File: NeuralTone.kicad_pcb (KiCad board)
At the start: 2 copper layers, 89 parts, among them J1 USB C, J2 Guitar, J3 Headphones, J4 USB Port, J5 Line Out, J6 TF-01A, J7 DF40HC(3.0)-100DS, J8 DF40HC(3.0)-100DS, Q1 AON7421, SW1 SW_Push, U1 AP2125N-3.3, U2 CH224K, U3 MCP6022, U4 AP2125N-3.3, U5 AP2151, U6 NAU8814YG, U7 DRTR5V0U2SR, Y1 OT322512MJBA4SL

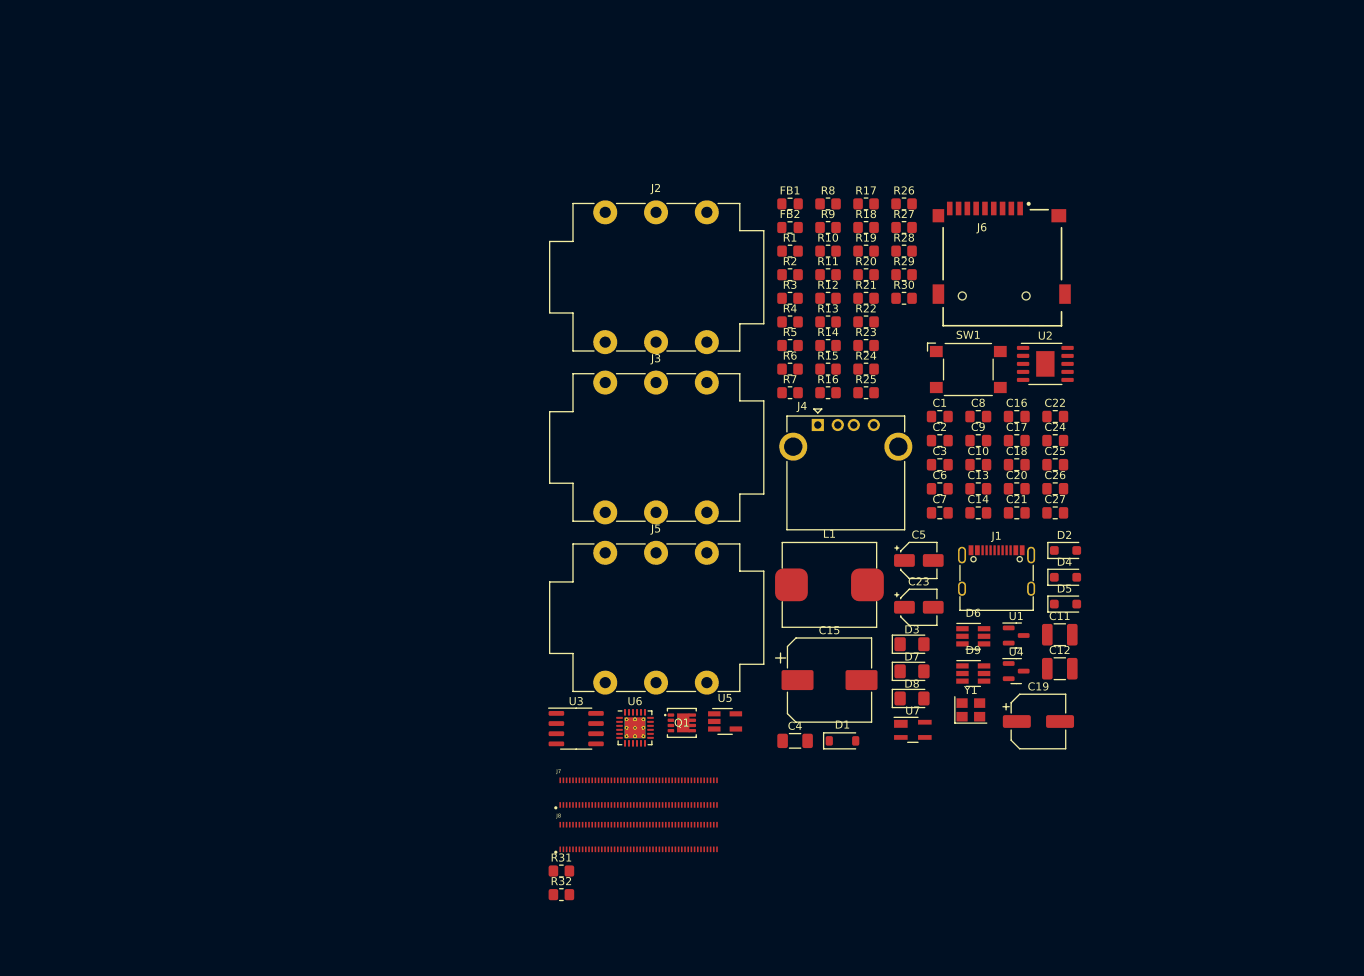
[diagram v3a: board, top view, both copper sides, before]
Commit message: fan control and other updates
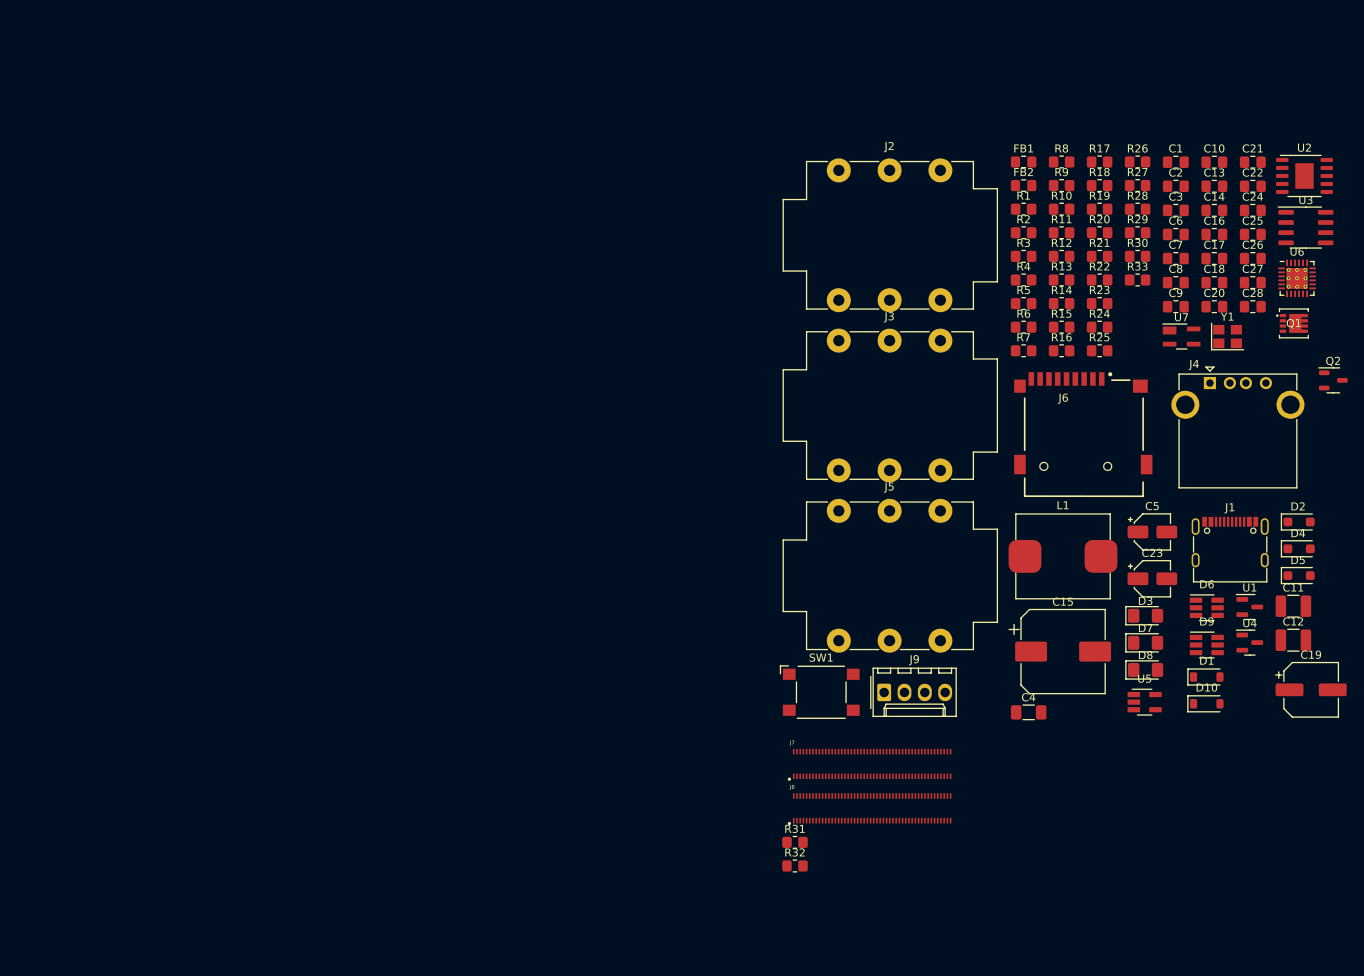
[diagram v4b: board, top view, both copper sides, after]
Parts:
- added C28: 100n, Capacitor_SMD:C_0805_2012Metric_Pad1.18x1.45mm_HandSolder, F.Cu at (205.4, 61.7)
- added D10: 1N4148W, Diode_SMD:D_SOD-123, F.Cu at (199.6, 111.4)
- added J9: Conn_01x04, Connector_Molex:Molex_KK-254_AE-6410-04A_1x04_P2.54mm_Vertical, F.Cu at (159.3, 110.0)
- added Q2: IRLML6344, Package_TO_SOT_SMD:SOT-23-3, F.Cu at (215.5, 70.9)
- added R33: 10k, Resistor_SMD:R_0805_2012Metric_Pad1.20x1.40mm_HandSolder, F.Cu at (191.0, 58.4)
- C9: value 1u -> 100n
- R13: value 1k -> 470k
- R14: value 1.8k -> 10k
- moved U3 110.6 mm to (212.0, 51.8)
- moved U6 100.0 mm to (210.9, 58.2)
- moved Q1 91.4 mm to (210.5, 63.8)
- moved U7 59.5 mm to (196.5, 65.5)
- moved Y1 56.6 mm to (202.3, 65.5)
- moved C21 52.8 mm to (205.4, 43.7)
- moved U5 52.5 mm to (191.9, 111.2)
- moved J4 49.3 mm to (200.0, 71.3)
- moved C13 48.0 mm to (200.6, 46.7)
- moved C10 48.0 mm to (200.6, 43.7)
- moved C14 48.0 mm to (200.6, 49.7)
- moved D1 46.2 mm to (199.6, 108.0)
- moved SW1 44.3 mm to (151.5, 109.9)
- moved C2 43.4 mm to (195.8, 46.7)
- moved C1 43.4 mm to (195.8, 43.7)
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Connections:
- R9 pad 1: /VBUS -> RPI_PWM
- R9 pad 2: Net-(Q1-G) -> Net-(Q2-G)

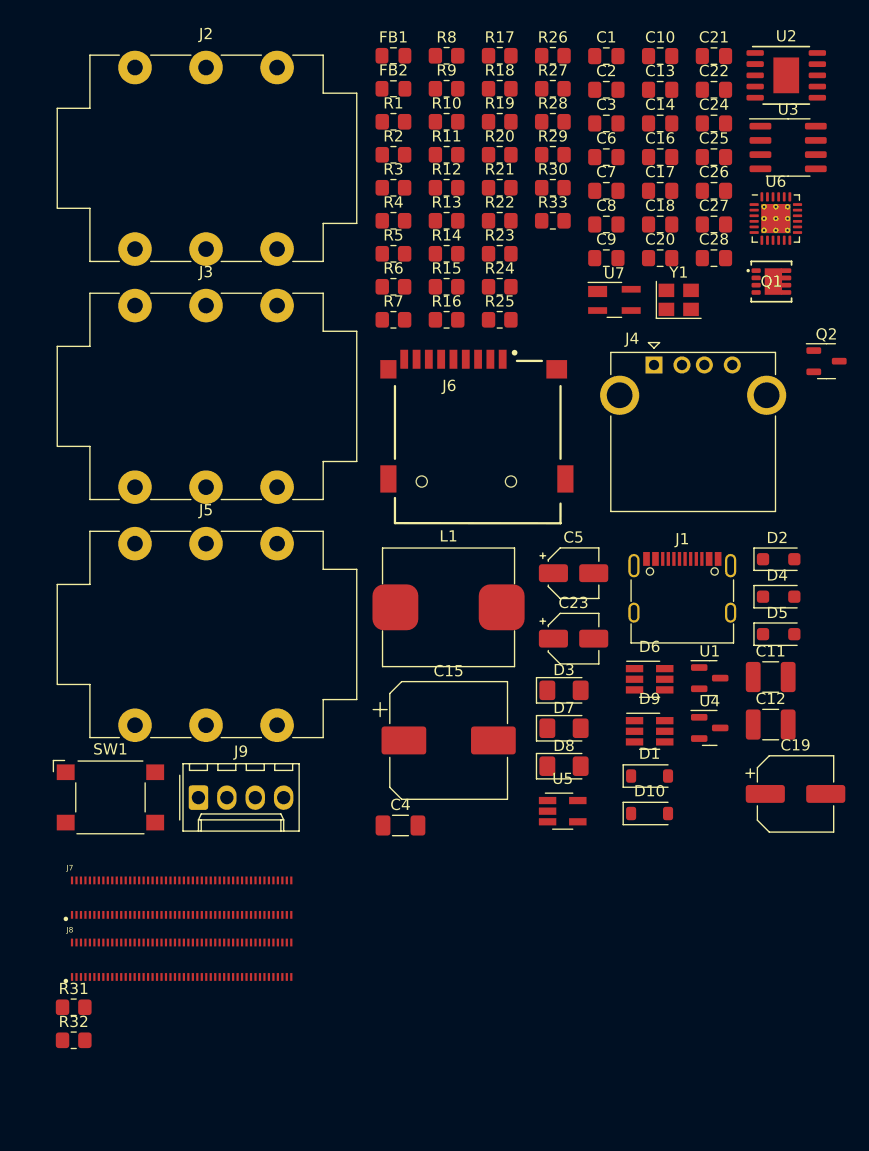
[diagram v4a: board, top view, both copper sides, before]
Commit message: fix speaker voltage and current switch diode
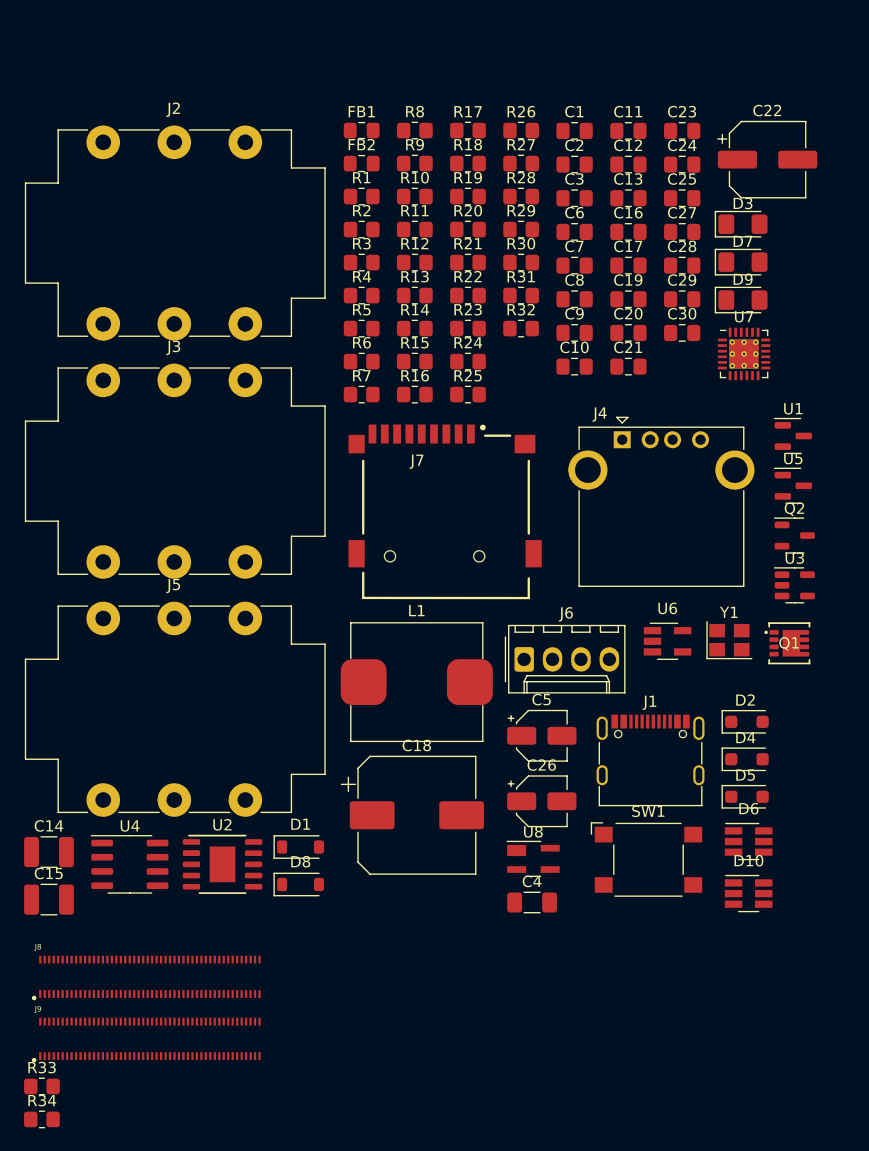
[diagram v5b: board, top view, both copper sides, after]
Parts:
- added C29: 100n, Capacitor_SMD:C_0805_2012Metric_Pad1.18x1.45mm_HandSolder, F.Cu at (202.6, 65.4)
- added C30: 4.7u, Capacitor_SMD:C_0805_2012Metric_Pad1.18x1.45mm_HandSolder, F.Cu at (202.6, 68.4)
- added R34: 330, Resistor_SMD:R_0805_2012Metric_Pad1.20x1.40mm_HandSolder, F.Cu at (145.3, 138.7)
- added U8: DRTR5V0U2SR, Package_TO_SOT_SMD:SOT-143_Handsoldering, F.Cu at (189.3, 115.4)
- C11: value 47u -> 100n; footprint Capacitor_SMD:C_1210_3225Metric_Pad1.33x2.70mm_HandSolder -> Capacitor_SMD:C_0805_2012Metric_Pad1.18x1.45mm_HandSolder
- C12: value 47u -> 1u; footprint Capacitor_SMD:C_1210_3225Metric_Pad1.33x2.70mm_HandSolder -> Capacitor_SMD:C_0805_2012Metric_Pad1.18x1.45mm_HandSolder
- C13: value 4.7u -> 1u
- C14: value 4.7u -> 47u; footprint Capacitor_SMD:C_0805_2012Metric_Pad1.18x1.45mm_HandSolder -> Capacitor_SMD:C_1210_3225Metric_Pad1.33x2.70mm_HandSolder
- C15: value 470u -> 47u; footprint Capacitor_SMD:CP_Elec_10x10 -> Capacitor_SMD:C_1210_3225Metric_Pad1.33x2.70mm_HandSolder
- C16, C17, C24, C25: value 33p -> 4.7u
- C18: value 4.7u -> 2200u; footprint Capacitor_SMD:C_0805_2012Metric_Pad1.18x1.45mm_HandSolder -> Capacitor_SMD:CP_Elec_10x10
- C19: value 150u -> 33p; footprint Capacitor_SMD:CP_Elec_6.3x7.7 -> Capacitor_SMD:C_0805_2012Metric_Pad1.18x1.45mm_HandSolder
- C20, C27: value 4.7u -> 33p
- C22: value 4.7u -> 150u; footprint Capacitor_SMD:C_0805_2012Metric_Pad1.18x1.45mm_HandSolder -> Capacitor_SMD:CP_Elec_6.3x7.7
- C23: footprint Capacitor_SMD:CP_Elec_4x5.3 -> Capacitor_SMD:C_0805_2012Metric_Pad1.18x1.45mm_HandSolder
- C26: value 100n -> 4.7u; footprint Capacitor_SMD:C_0805_2012Metric_Pad1.18x1.45mm_HandSolder -> Capacitor_SMD:CP_Elec_4x5.7
- C28: value 100n -> 33p
- C5: footprint Capacitor_SMD:CP_Elec_4x5.3 -> Capacitor_SMD:CP_Elec_4x5.7
- D10: value 1N4148W -> PESD3V3S4UD; footprint Diode_SMD:D_SOD-123 -> Package_TO_SOT_SMD:SOT-23-6_Handsoldering
- D8: value LED_Small -> 1N4148W; footprint LED_SMD:LED_1206_3216Metric_Pad1.42x1.75mm_HandSolder -> Diode_SMD:D_SOD-123
- D9: value PESD3V3S4UD -> LED_Small; footprint Package_TO_SOT_SMD:SOT-23-6_Handsoldering -> LED_SMD:LED_1206_3216Metric_Pad1.42x1.75mm_HandSolder
- J1: value USB C -> USB-C PD
- J4: value USB Port -> USB-A Port
- J6: value TF-01A -> 5V Fan; footprint NeuralTone:TF-01A -> Connector_Molex:Molex_KK-254_AE-6410-04A_1x04_P2.54mm_Vertical
- J7: value DF40HC(3.0)-100DS -> TF-01A; footprint NeuralTone:DF40HC(3.0)-100DS_A -> NeuralTone:TF-01A
- J8: footprint NeuralTone:DF40HC(3.0)-100DS_B -> NeuralTone:DF40HC(3.0)-100DS_A
- J9: value Conn_01x04 -> DF40HC(3.0)-100DS; footprint Connector_Molex:Molex_KK-254_AE-6410-04A_1x04_P2.54mm_Vertical -> NeuralTone:DF40HC(3.0)-100DS_B
- R21: value 10k -> 470k
- R31: value 330 -> 1k
- R32: value 330 -> 10k
- R33: value 10k -> 330
- R6: value 2.2M -> 470k
- R7: value 10k -> 2.2M
- R9: value 1k -> 10k
- U3: value MCP6022 -> TLV70245; footprint Package_SO:SOIC-8_3.9x4.9mm_P1.27mm -> Package_TO_SOT_SMD:SOT-23-5
- U4: value AP2125N-3.3 -> MCP6022; footprint Package_TO_SOT_SMD:SOT-23 -> Package_SO:SOIC-8_3.9x4.9mm_P1.27mm
- U5: value AP2151 -> AP2125N-3.3; footprint Package_TO_SOT_SMD:SOT-23-5_HandSoldering -> Package_TO_SOT_SMD:SOT-23
- U6: value NAU8814YG -> AP2151; footprint Package_DFN_QFN:QFN-24-1EP_4x4mm_P0.5mm_EP2.6x2.6mm_ThermalVias -> Package_TO_SOT_SMD:SOT-23-5_HandSoldering
- U7: value DRTR5V0U2SR -> NAU8814YG; footprint Package_TO_SOT_SMD:SOT-143_Handsoldering -> Package_DFN_QFN:QFN-24-1EP_4x4mm_P0.5mm_EP2.6x2.6mm_ThermalVias
- moved R33 89.8 mm to (145.3, 135.8)
- moved U2 86.7 mm to (161.5, 115.9)
- moved C14 85.0 mm to (146.0, 114.8)
- moved R31 75.1 mm to (188.2, 65.1)
- moved R32 75.1 mm to (188.2, 68.0)
- moved C18 57.1 mm to (178.8, 111.5)
- moved C26 56.7 mm to (190.0, 110.3)
- moved U4 53.2 mm to (153.2, 115.9)
- moved C12 51.6 mm to (197.8, 53.4)
- moved C11 50.4 mm to (197.8, 50.4)
- moved SW1 48.4 mm to (199.5, 115.5)
- moved C19 46.7 mm to (197.8, 65.4)
- moved C23 46.4 mm to (202.6, 50.4)
- moved D3 44.6 mm to (208.0, 58.7)
- moved D7 44.6 mm to (208.0, 62.1)
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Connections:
- C10 pad 1: GND -> Net-(Q1-D)
- C10 pad 2: +3V3A_B -> Net-(Q1-G)
- C11 pad 1: Net-(C11-Pad1) -> GND
- C11 pad 2: GND -> +3V3A_B
- C12 pad 1: Net-(C12-Pad1) -> +5V
- C14 pad 1: +3V3A_C -> Net-(C14-Pad1)
- C15 pad 1: /HEADPHONES -> Net-(C15-Pad1)
- C15 pad 2: Net-(C15-Pad2) -> GND
- C16 pad 1: GND -> +3V3A_C
- C16 pad 2: Net-(C15-Pad2) -> GND
- C17 pad 1: GND -> +3V3A_S
- C17 pad 2: Net-(C17-Pad2) -> GND
- C18 pad 1: GND -> /HEADPHONES
- C18 pad 2: Net-(U6-VREF) -> Net-(C18-Pad2)
- C19 pad 1: Net-(J4-VBUS) -> GND
- C19 pad 2: GND -> Net-(C18-Pad2)
- C20 pad 1: +3V3 -> GND
- C20 pad 2: GND -> Net-(C20-Pad2)
- C21 pad 1: +3V3 -> GND
- C21 pad 2: GND -> Net-(U7-VREF)
- C22 pad 1: +5V -> Net-(J4-VBUS)
- C23 pad 1: /LINE_OUT -> +3V3
- C23 pad 2: Net-(C23-Pad2) -> GND
- C24 pad 1: GND -> +3V3
- C24 pad 2: Net-(C23-Pad2) -> GND
- C25 pad 1: GND -> +5V
- C25 pad 2: Net-(C25-Pad2) -> GND
- C26 pad 1: +3V3 -> /LINE_OUT
- C26 pad 2: GND -> Net-(C26-Pad2)
- C27 pad 1: +3V3 -> GND
- C27 pad 2: GND -> Net-(C26-Pad2)
- C28 pad 1: /VBUS -> GND
- C28 pad 2: Net-(Q1-G) -> Net-(C28-Pad2)
- C4 pad 2: Net-(U3B-+) -> Net-(U4B-+)
- C5 pad 1: Net-(U3B--) -> Net-(U4B--)
- C7 pad 1: +3V3A_C -> +3V3A_S
- C8 pad 2: Net-(U3A-+) -> Net-(U4A-+)
- C9 pad 1: Net-(Q1-D) -> /VBUS
- D10 pad 1: +5V -> Net-(J7-CLK)
- D10 pad 2: /PWM -> GND
- D4 pad 2: Net-(C17-Pad2) -> Net-(C20-Pad2)
- D5 pad 2: Net-(C25-Pad2) -> Net-(C28-Pad2)
- D6 pad 1: Net-(J6-DAT2) -> Net-(J7-DAT2)
- D6 pad 3: Net-(J6-DAT3/CD) -> Net-(J7-DAT3/CD)
- D6 pad 4: Net-(J6-CMD) -> Net-(J7-CMD)
- D8 pad 1: GND -> +5V
- D8 pad 2: Net-(D8-A) -> /PWM
- D9 pad 1: Net-(J6-CLK) -> GND
- D9 pad 2: GND -> Net-(D9-A)
- FB1 pad 1: Net-(C15-Pad2) -> Net-(C18-Pad2)
- FB1 pad 2: Net-(C17-Pad2) -> Net-(C20-Pad2)
- FB2 pad 1: Net-(C23-Pad2) -> Net-(C26-Pad2)
- FB2 pad 2: Net-(C25-Pad2) -> Net-(C28-Pad2)
- J3 pad R: Net-(C17-Pad2) -> Net-(C20-Pad2)
- J3 pad T: Net-(C17-Pad2) -> Net-(C20-Pad2)
- J5 pad R: Net-(C25-Pad2) -> Net-(C28-Pad2)
- J5 pad T: Net-(C25-Pad2) -> Net-(C28-Pad2)
- J6 pad 1: Net-(J6-DAT2) -> GND
- J6 pad 2: Net-(J6-DAT3/CD) -> +5V
- J6 pad 3: Net-(J6-CMD) -> unconnected-(J6-Pin_3-Pad3)
- J6 pad 4: +3V3 -> /PWM
- J7 pad 1: GND -> Net-(J7-DAT2)
- J7 pad 2: GND -> Net-(J7-DAT3/CD)
- J7 pad 3: unconnected-(J7-Ethernet_Pair3_P-Pad3) -> Net-(J7-CMD)
- J7 pad 4: unconnected-(J7-Ethernet_Pair1_P-Pad4) -> +3V3
- J7 pad 5: unconnected-(J7-Ethernet_Pair3_N-Pad5) -> Net-(J7-CLK)
- J7 pad 6: unconnected-(J7-Ethernet_Pair1_N-Pad6) -> GND
- J7 pad 7: GND -> Net-(J7-DAT0)
- J7 pad 8: GND -> Net-(J7-DAT1)
- J7 pad 9: unconnected-(J7-Ethernet_Pair2_N-Pad9) -> GND
- R10 pad 2: Net-(C11-Pad1) -> Net-(C14-Pad1)
- R11 pad 2: Net-(C12-Pad1) -> Net-(C15-Pad1)
- R14 pad 1: Net-(C15-Pad2) -> Net-(C18-Pad2)
- R15 pad 2: Net-(U5-EN) -> Net-(U6-EN)
- R16 pad 2: Net-(U6-ADCOUT) -> Net-(U7-ADCOUT)
- R17 pad 2: Net-(U6-DACIN) -> Net-(U7-DACIN)
- R18 pad 2: Net-(U6-FS) -> Net-(U7-FS)
- R19 pad 2: Net-(U6-BCLK) -> Net-(U7-BCLK)
- R20 pad 1: Net-(U6-MODE) -> Net-(U7-MODE)
- R21 pad 1: Net-(C23-Pad2) -> Net-(C26-Pad2)
- R22 pad 2: Net-(U6-CSb/GPIO) -> Net-(U7-CSb/GPIO)
- R23 pad 2: Net-(J6-DAT2) -> Net-(J7-DAT2)
- R25 pad 2: Net-(J6-DAT3/CD) -> Net-(J7-DAT3/CD)
- R26 pad 2: Net-(J6-CMD) -> Net-(J7-CMD)
- R27 pad 2: Net-(D8-A) -> Net-(D9-A)
- R28 pad 2: Net-(J6-CLK) -> Net-(J7-CLK)
- R29 pad 2: Net-(J6-DAT0) -> Net-(J7-DAT0)
- R30 pad 2: Net-(J6-DAT1) -> Net-(J7-DAT1)
- R31 pad 1: I2C_SCL -> FAN_PWM
- R31 pad 2: Net-(J7-GPIO3) -> Net-(Q2-G)
- R32 pad 1: I2C_SDA -> Net-(Q2-G)
- R32 pad 2: Net-(J7-GPIO2) -> GND
- R33 pad 1: Net-(Q2-G) -> I2C_SCL
- R33 pad 2: GND -> Net-(J8-GPIO3)
- R5 pad 1: GND -> +5V
- R5 pad 2: CODEC_AUX -> Net-(U3-EN)
- R6 pad 1: Net-(U3A--) -> CODEC_AUX
- R6 pad 2: Net-(U3B-+) -> GND
- R7 pad 1: Net-(U3A-+) -> Net-(U4A--)
- R7 pad 2: +3V3A_B -> Net-(U4B-+)
- R8 pad 1: GND -> Net-(U4A-+)
- R8 pad 2: Net-(U3A-+) -> +3V3A_B
- R9 pad 1: RPI_PWM -> GND
- R9 pad 2: Net-(Q2-G) -> Net-(U4A-+)
- U3 pad 1: Net-(U3A--) -> +5V
- U3 pad 2: Net-(U3A--) -> GND
- U3 pad 3: Net-(U3A-+) -> Net-(U3-EN)
- U3 pad 4: GND -> unconnected-(U3-NC-Pad4)
- U3 pad 5: Net-(U3B-+) -> +3V3A_S
- U4 pad 1: GND -> Net-(U4A--)
- U4 pad 2: +3V3A_C -> Net-(U4A--)
- U4 pad 3: +5V -> Net-(U4A-+)
- U5 pad 1: Net-(J4-VBUS) -> GND
- U5 pad 2: GND -> +3V3A_C
- U5 pad 3: unconnected-(U5-~{FLG}-Pad3) -> +5V
- U6 pad 1: unconnected-(U6-MICBIAS-Pad1) -> Net-(J4-VBUS)
- U6 pad 2: +3V3A_C -> GND
- U6 pad 3: GND -> unconnected-(U6-~{FLG}-Pad3)
- U6 pad 4: +3V3 -> Net-(U6-EN)
- U6 pad 5: +3V3 -> +5V
- U7 pad 1: GND -> unconnected-(U7-MICBIAS-Pad1)
- U7 pad 2: USBD+ -> +3V3A_C
- U7 pad 3: USBD- -> GND
- U7 pad 4: Net-(J4-VBUS) -> +3V3
